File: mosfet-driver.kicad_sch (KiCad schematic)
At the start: 21 parts, among them J4 Conn_01x02, J5 Conn_01x02, Q2 IRF3205, Q3 MMBT3904, Q4 MMBT3904, U4 DRV8876RGTR

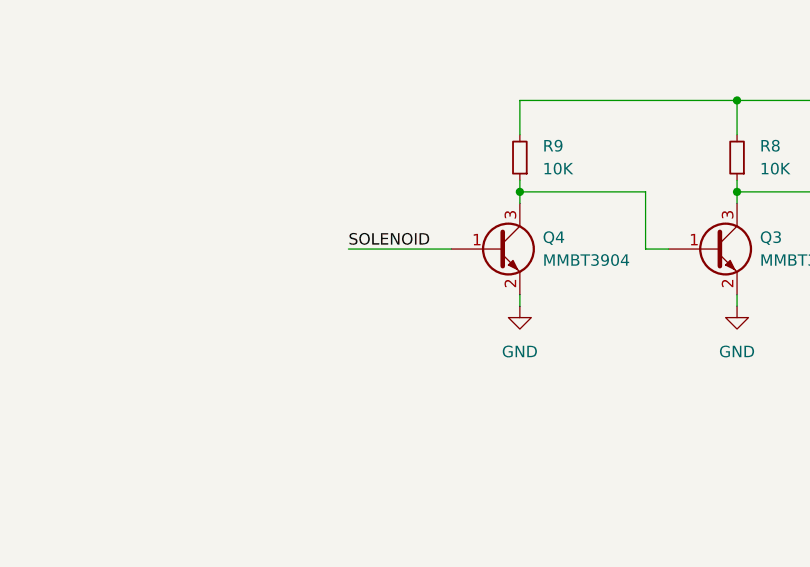
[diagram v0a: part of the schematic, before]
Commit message: Added footwitch, usb led activity
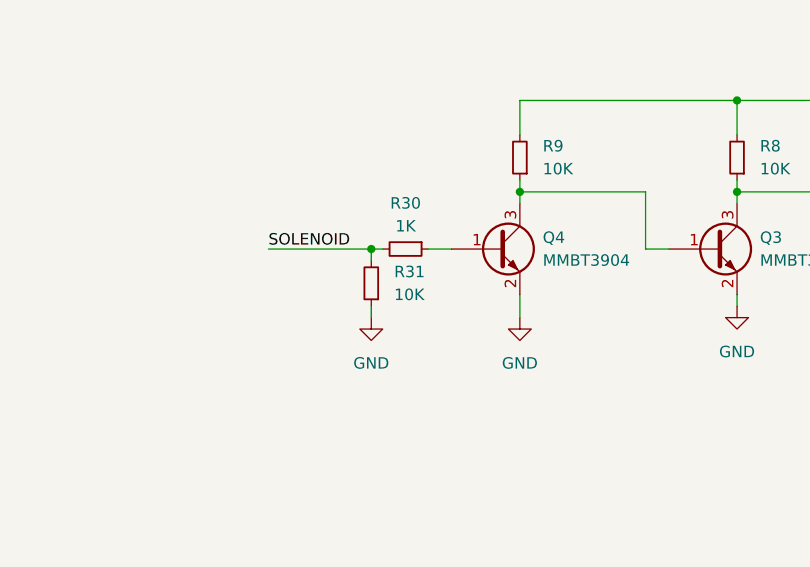
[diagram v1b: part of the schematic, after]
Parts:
- added R30: 1K, Resistor_SMD:R_0603_1608Metric, symbol Device:R_Small
- added R31: 10K, Resistor_SMD:R_0603_1608Metric, symbol Device:R_Small
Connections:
- net GND: now also R31.1
- net SOLENOID: now also R30.2, R31.2; no longer Q4.1 (B)
- new net: Q4.1 (B), R30.1

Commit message: layouting Power, Motor section
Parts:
- C9: footprint Capacitor_SMD:C_0603_1608Metric -> Capacitor_THT:CP_Radial_D6.3mm_P2.50mm
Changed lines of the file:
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@@
 			)
 		)
-		(property "Footprint" "Capacitor_SMD:C_0603_1608Metric"
+		(property "Footprint" "Capacitor_THT:CP_Radial_D6.3mm_P2.50mm"
 			(at 51.7652 115.57 0)
 			(effects

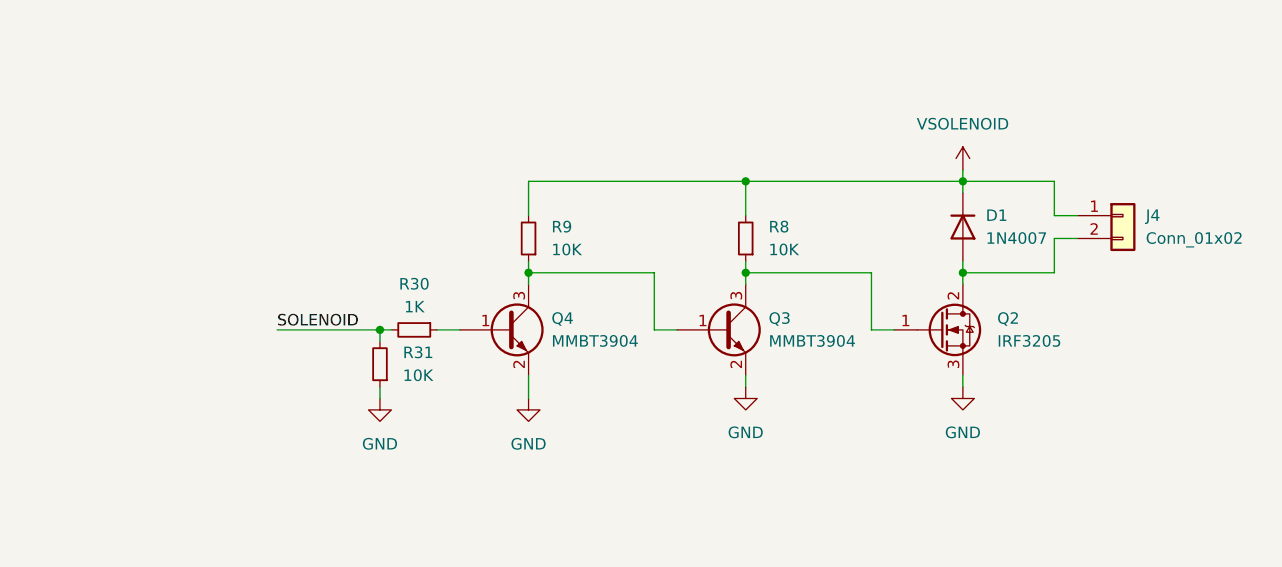
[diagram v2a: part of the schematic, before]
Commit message: Added push button connector
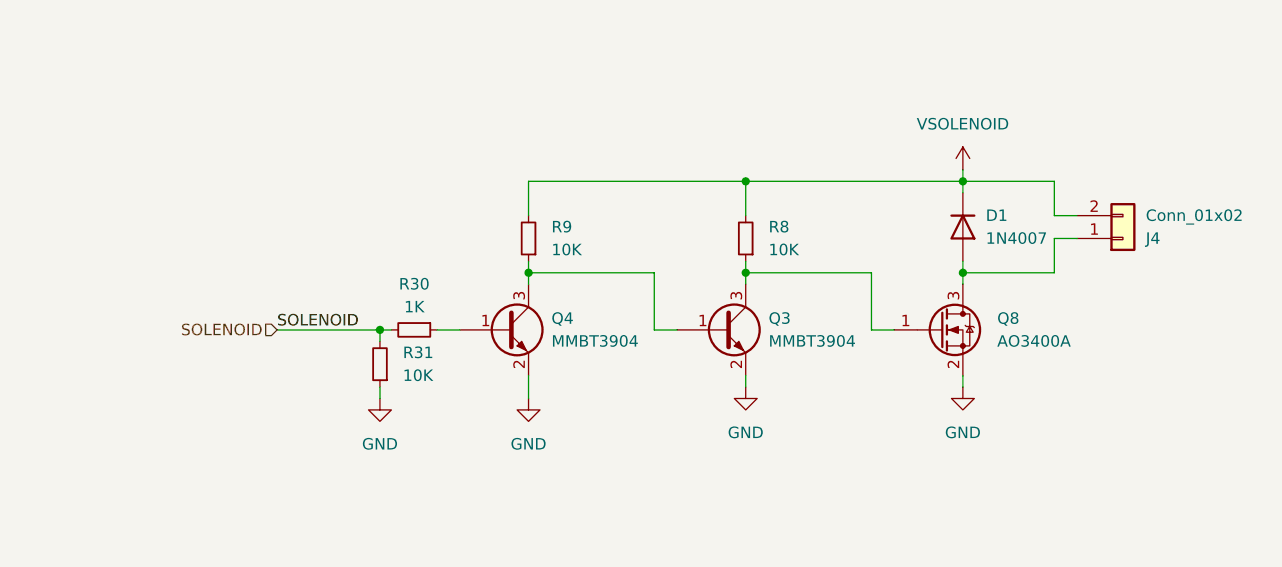
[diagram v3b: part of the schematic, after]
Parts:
- removed Q2: IRF3205, Package_TO_SOT_THT:TO-220-3_Vertical, symbol Transistor_FET:IRF3205
- added Q8: AO3400A, Package_TO_SOT_SMD:SOT-23, symbol Transistor_FET:AO3400A
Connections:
- net GND: now also Q8.2 (S)
- net VSOLENOID: now also J4.2 (Pin_2); no longer J4.1 (Pin_1)
- net at Q3.3 (C), R8.1: now also Q8.1 (G)
- net at D1.2 (A): now also J4.1 (Pin_1), Q8.3 (D); no longer J4.2 (Pin_2)
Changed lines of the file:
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@@
 	(label "VREF"
 		(at 67.31 64.77 0)
-		(fields_autoplaced yes)
 		(effects
 			(font
@@
 	(label "NFAULT"
 		(at 67.31 85.09 0)
-		(fields_autoplaced yes)
 		(effects
 			(font
@@
 	(label "PH/IN2"
 		(at 67.31 62.23 0)
-		(fields_autoplaced yes)
 		(effects
 			(font
@@
 	(label "PMODE"
 		(at 67.31 95.25 0)
-		(fields_autoplaced yes)
 		(effects
 			(font
@@
 	(label "VREF"
 		(at 43.18 67.31 180)
-		(fields_autoplaced yes)
 		(effects
 			(font
@@
 	(label "EN/IN1"
 		(at 67.31 57.15 0)
-		(fields_autoplaced yes)
 		(effects
 			(font
@@
 	(label "NSLEEP"
 		(at 67.31 90.17 0)
-		(fields_autoplaced yes)
 		(effects
 			(font
@@
 	(label "IMODE"
 		(at 67.31 80.01 0)
-		(fields_autoplaced yes)
 		(effects
 			(font
@@
 	(label "PMODE"
 		(at 111.76 137.16 180)
-		(fields_autoplaced yes)
 		(effects
 			(font
@@
 	(label "SOLENOID"
 		(at 166.37 104.14 0)
-		(fields_autoplaced yes)
 		(effects
 			(font
@@
 		)
 	)
+	(hierarchical_label "SOLENOID"
+		(shape input)
+		(at 166.37 104.14 180)
+		(effects
+			(font
+				(size 1.27 1.27)
+			)
+			(justify right)
+		)
+	)
 	(symbol
 		(lib_id "power:GND")
@@
 	)
 	(symbol
-		(lib_id "Transistor_FET:IRF3205")
-		(at 240.03 104.14 0)
-		(unit 1)
-		(exclude_from_sim no)
-		(in_bom yes)
-		(on_board yes)
-		(dnp no)
-		(fields_autoplaced yes)
-		(property "Reference" "Q2"
-			(at 246.38 102.8699 0)
-			(effects
-				(font
-					(size 1.27 1.27)
-				)
-				(justify left)
-			)
-		)
-		(property "Value" "IRF3205"
-			(at 246.38 105.4099 0)
-			(effects
-				(font
-					(size 1.27 1.27)
-				)
-				(justify left)
-			)
-		)
-		(property "Footprint" "Package_TO_SOT_THT:TO-220-3_Vertical"
-			(at 245.11 106.045 0)
-			(effects
-				(font
-					(size 1.27 1.27)
-					(italic yes)
-				)
-				(justify left)
-				(hide yes)
-			)
-		)
-		(property "Datasheet" "http://www.irf.com/product-info/datasheets/data/irf3205.pdf"
-			(at 245.11 107.95 0)
-			(effects
-				(font
-					(size 1.27 1.27)
-				)
-				(justify left)
-				(hide yes)
-			)
-		)
-		(property "Description" "110A Id, 55V Vds, Single N-Channel HEXFET Power MOSFET, 8mOhm Ron, TO-220AB"
-			(at 240.03 104.14 0)
-			(effects
-				(font
-					(size 1.27 1.27)
-				)
-				(hide yes)
-			)
-		)
-		(pin "2"
-		)
-		(pin "1"
-		)
-		(pin "3"
-		)
-		(instances
-			(project ""
-				(path "/58f4f64d-10fe-43f6-8af4-d87642e52b35/76adc4ea-8174-4821-81c1-63e0db9c24d0"
-					(reference "Q2")
-					(unit 1)
-				)
-			)
-		)
-	)
-	(symbol
 		(lib_id "power:GND")
 		(at 177.8 111.76 0)
@@
 	(symbol
 		(lib_id "Connector_Generic:Conn_01x02")
-		(at 260.35 91.44 0)
-		(unit 1)
-		(exclude_from_sim no)
-		(in_bom yes)
-		(on_board yes)
-		(dnp no)
-		(fields_autoplaced yes)
+		(at 260.35 93.98 0)
+		(mirror x)
+		(unit 1)
+		(exclude_from_sim no)
+		(in_bom yes)
+		(on_board yes)
+		(dnp no)
 		(property "Reference" "J4"
-			(at 262.89 91.4399 0)
+			(at 262.89 93.9801 0)
 			(effects
 				(font
@@
 		)
 		(property "Value" "Conn_01x02"
-			(at 262.89 93.9799 0)
+			(at 262.89 91.4401 0)
 			(effects
 				(font
@@
 		)
 		(property "Footprint" "Connector_JST:JST_PH_B2B-PH-K_1x02_P2.00mm_Vertical"
-			(at 260.35 91.44 0)
+			(at 260.35 93.98 0)
 			(effects
 				(font
@@
 		)
 		(property "Datasheet" "~"
-			(at 260.35 91.44 0)
+			(at 260.35 93.98 0)
 			(effects
 				(font
@@
 		)
 		(property "Description" "Generic connector, single row, 01x02, script generated (kicad-library-utils/schlib/autogen/connector/)"
-			(at 260.35 91.44 0)
+			(at 260.35 93.98 0)
 			(effects
 				(font
@@
 					(unit 1)
 				)
+			)
+		)
+	)
+	(symbol
+		(lib_id "Transistor_FET:AO3400A")
+		(at 240.03 104.14 0)
+		(unit 1)
+		(exclude_from_sim no)
+		(in_bom yes)
+		(on_board yes)
+		(dnp no)
+		(fields_autoplaced yes)
+		(property "Reference" "Q8"
+			(at 246.38 102.8699 0)
+			(effects
+				(font
+					(size 1.27 1.27)
+				)
+				(justify left)
+			)
+		)
+		(property "Value" "AO3400A"
+			(at 246.38 105.4099 0)
+			(effects
+				(font
+					(size 1.27 1.27)
+				)
+				(justify left)
+			)
+		)
+		(property "Footprint" "Package_TO_SOT_SMD:SOT-23"
+			(at 245.11 106.045 0)
+			(effects
+				(font
+					(size 1.27 1.27)
+					(italic yes)
+				)
+				(justify left)
+				(hide yes)
+			)
+		)
+		(property "Datasheet" "http://www.aosmd.com/pdfs/datasheet/AO3400A.pdf"
+			(at 245.11 107.95 0)
+			(effects
+				(font
+					(size 1.27 1.27)
+				)
+				(justify left)
+				(hide yes)
+			)
+		)
+		(property "Description" "30V Vds, 5.7A Id, N-Channel MOSFET, SOT-23"
+			(at 240.03 104.14 0)
+			(effects
+				(font
+					(size 1.27 1.27)
+				)
+				(hide yes)
+			)
+		)
+		(pin "3"
+		)
+		(pin "1"
+		)
+		(pin "2"
+		)
+		(instances
+			(project ""
+				(path "/58f4f64d-10fe-43f6-8af4-d87642e52b35/76adc4ea-8174-4821-81c1-63e0db9c24d0"
+					(reference "Q8")
+					(unit 1)
+				)
